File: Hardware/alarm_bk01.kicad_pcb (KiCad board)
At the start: 2 copper layers, 65 x 22 mm, 18 parts, among them Q1 2N3904, SW1 START, SW2 Sensor, SW3 SW_SPDT, U1 ATtiny85V-10P

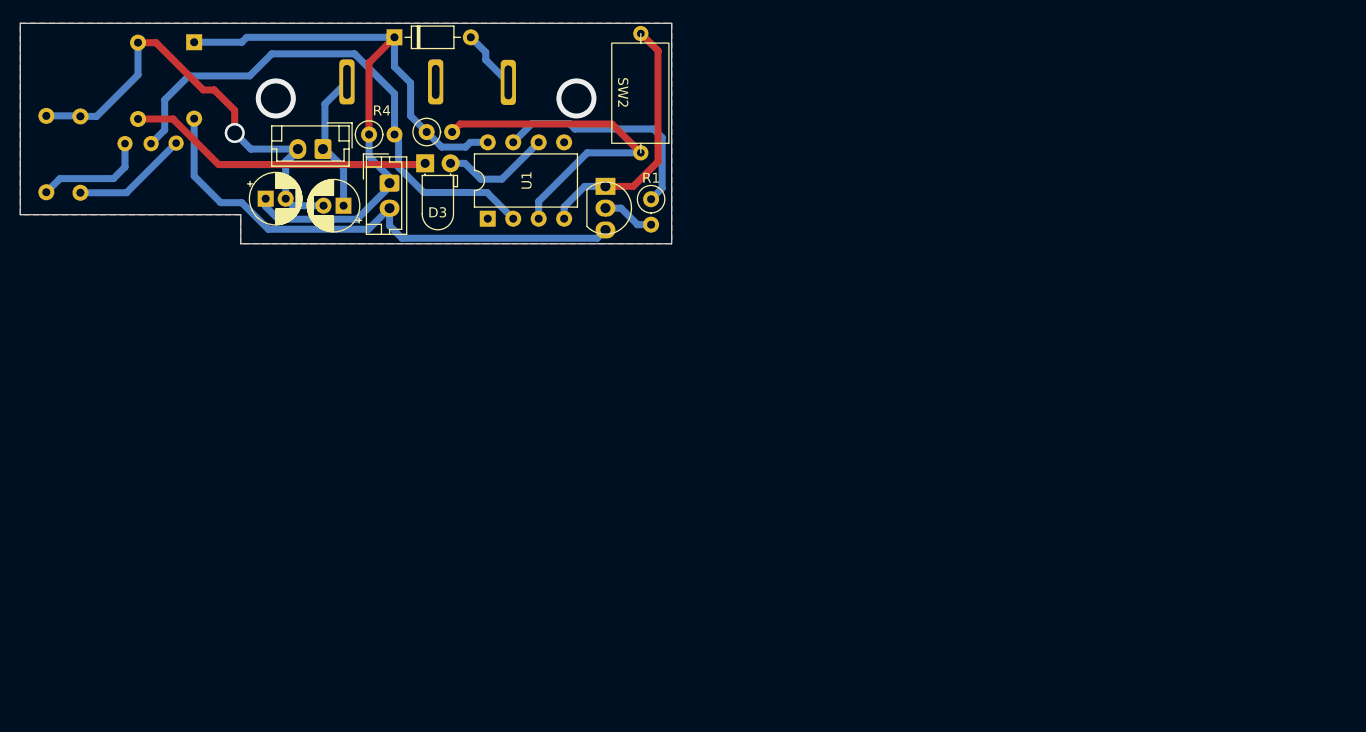
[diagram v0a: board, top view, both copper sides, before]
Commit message: add smd design file
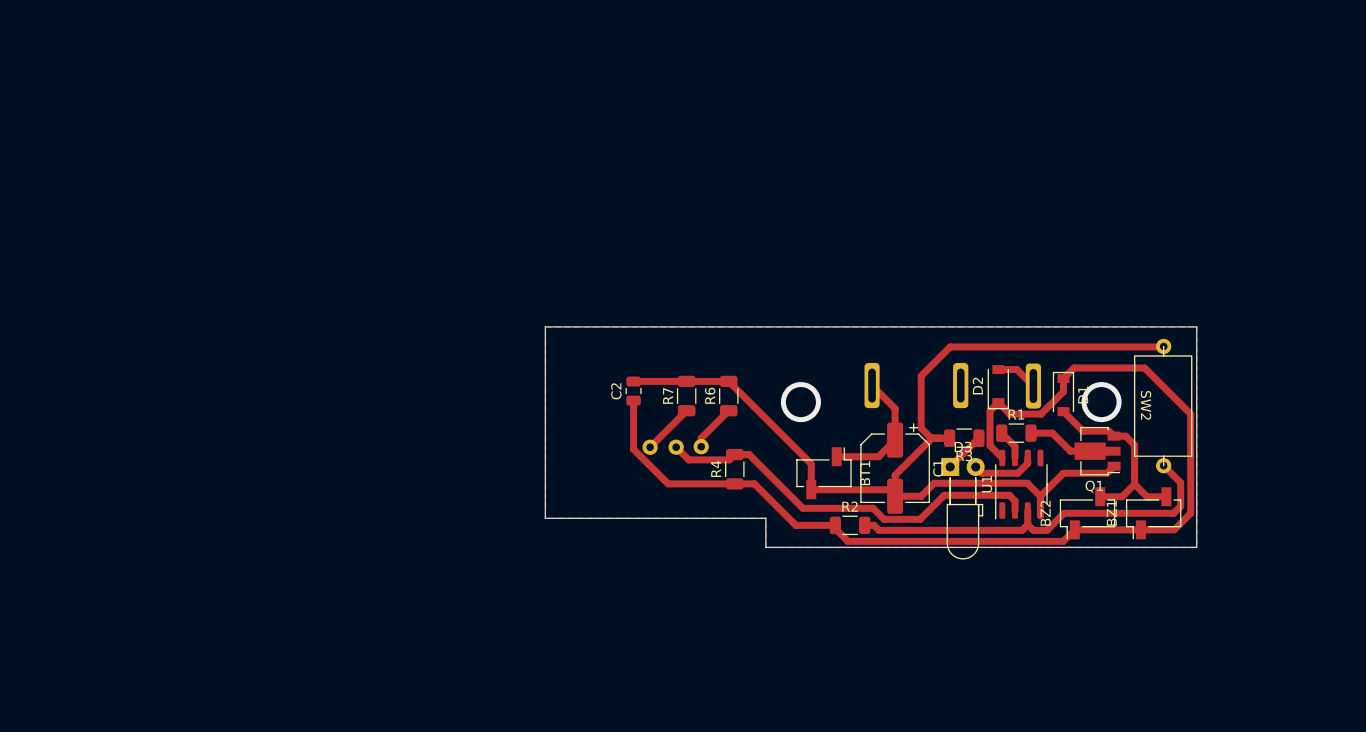
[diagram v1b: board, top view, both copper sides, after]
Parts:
- added BZ2: Buzzer, Connector_PinSocket_2.54mm:PinSocket_1x02_P2.54mm_Vertical_SMD_Pin1Left, F.Cu at (164.3, 80.2)
- BT1, BZ1: footprint Connector_JST:JST_EH_B2B-EH-A_1x02_P2.50mm_Vertical -> Connector_PinSocket_2.54mm:PinSocket_1x02_P2.54mm_Vertical_SMD_Pin1Left
- C1: footprint Capacitor_THT:CP_Radial_D5.0mm_P2.00mm -> Capacitor_SMD:CP_Elec_6.3x5.4
- C2: value 47u -> 47uF; footprint Capacitor_THT:CP_Radial_D5.0mm_P2.00mm -> Capacitor_SMD:C_0805_2012Metric
- D1: footprint Diode_THT:D_DO-35_SOD27_P7.62mm_Horizontal -> Diode_SMD:D_SOD-123; moved to F.Cu
- D2: footprint Diode_THT:D_DO-35_SOD27_P7.62mm_Horizontal -> Diode_SMD:D_SOD-123
- D3: footprint LED_THT:LED_D3.0mm_Horizontal_O1.27mm_Z2.0mm -> LED_THT:LED_D3.0mm_Horizontal_O3.81mm_Z2.0mm
- Q1: footprint custom:TO-92_with_space -> Package_TO_SOT_SMD:SOT-89-3
- R1, R2, R4: footprint Resistor_THT:R_Axial_DIN0207_L6.3mm_D2.5mm_P2.54mm_Vertical -> Resistor_SMD:R_1206_3216Metric
- R3, R6, R7: footprint Resistor_THT:R_Axial_DIN0207_L6.3mm_D2.5mm_P7.62mm_Horizontal -> Resistor_SMD:R_1206_3216Metric; moved to F.Cu
- U1: footprint Package_DIP:DIP-8_W7.62mm -> Package_SO:SOP-8_3.9x4.9mm_P1.27mm
- moved D1 93.6 mm to (161.9, 68.4)
- moved R3 88.4 mm to (152.0, 72.7), turned to 180 degrees
- moved BZ1 83.1 mm to (170.9, 80.2), turned to 90 degrees
- moved D2 69.6 mm to (155.4, 67.5), turned to 90 degrees
- moved R6 67.8 mm to (128.5, 68.5)
- moved R7 67.1 mm to (124.3, 68.5)
- moved C1 61.0 mm to (145.1, 75.7), turned to -90 degrees
- moved SW2 60.8 mm to (171.9, 69.5)
- moved D3 60.5 mm to (150.6, 75.6)
- moved SW3 60.5 mm to (123.2, 76.2)
- moved SW1 60.5 mm to (151.6, 67.5)
- moved BT1 59.6 mm to (138.0, 76.2), turned to -90 degrees
- moved U1 59.5 mm to (157.7, 77.3)
- moved R2 57.7 mm to (140.6, 81.4)
- moved Q1 55.3 mm to (165.3, 74.0), turned to 180 degrees
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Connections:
- SW1 pad COM: /POWER -> (no net)
- SW1 pad NC: /ON_NET -> (no net)
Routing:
- net VCC: track 69.7 -> 106.3 mm
- net Net-(BZ1-Pad2): track 52.5 -> 19.9 mm
- net 0: track 73.6 -> 102.0 mm, vias 1 -> 0
- net Net-(D3-Pad1): track 30.6 -> 4.06 mm
- net alarma: track 22.8 -> 3.02 mm
- net sensibilidad: track 52.8 -> 39.4 mm
- net Net-(R6-Pad1): track 11.6 -> 4.73 mm
- net Net-(R7-Pad1): track 11.2 -> 5.16 mm
- net sensor: track 34.3 -> 39.5 mm
- net Indicator: track 11.0 -> 6.40 mm
- net Net-(Q1-Pad2): track 5.24 -> 8.95 mm
- net /ON_NET: track 6.05 -> 4.18 mm
- net /POWER: track 14.0 -> 12.9 mm
- removed copper zone on B.Cu, net 0

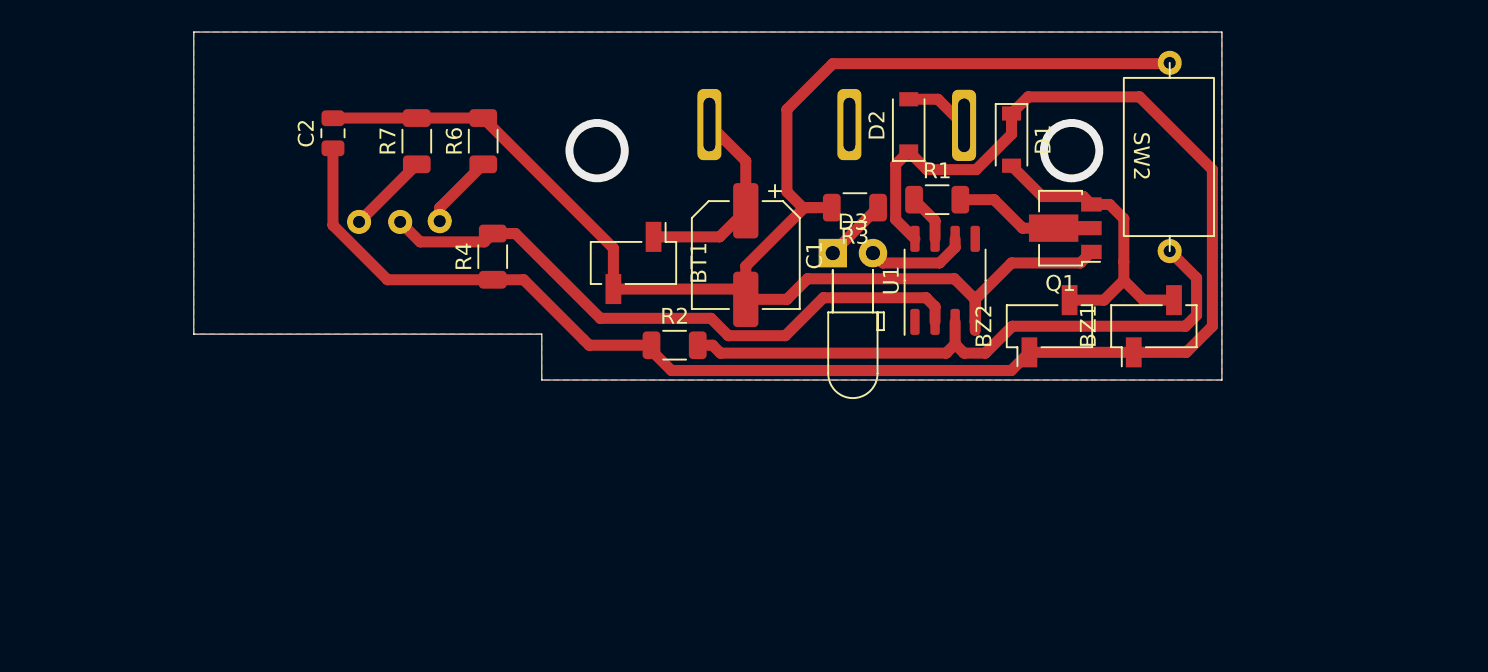
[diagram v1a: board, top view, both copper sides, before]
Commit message: pcb and holes of the new model
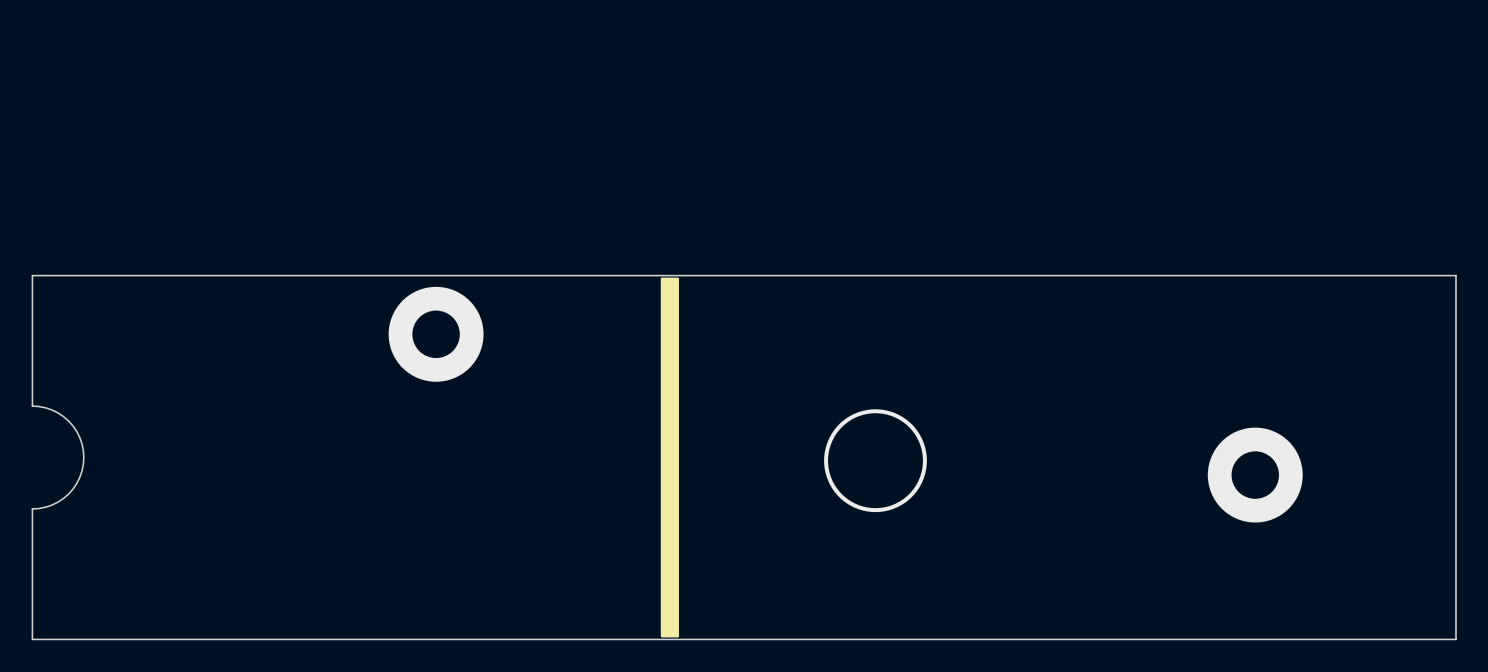
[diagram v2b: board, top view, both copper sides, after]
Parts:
- removed BT1: Battery, Connector_PinSocket_2.54mm:PinSocket_1x02_P2.54mm_Vertical_SMD_Pin1Left
- removed BZ1, BZ2: Buzzer, Connector_PinSocket_2.54mm:PinSocket_1x02_P2.54mm_Vertical_SMD_Pin1Left
- removed C1: 100u, Capacitor_SMD:CP_Elec_6.3x5.4
- removed C2: 47uF, Capacitor_SMD:C_0805_2012Metric
- removed D1, D2: 1N4148, Diode_SMD:D_SOD-123
- removed D3: LED, LED_THT:LED_D3.0mm_Horizontal_O3.81mm_Z2.0mm
- removed Q1: 2N3904, Package_TO_SOT_SMD:SOT-89-3
- removed R1: 180, Resistor_SMD:R_1206_3216Metric
- removed R2: 610k, Resistor_SMD:R_1206_3216Metric
- removed R3: 6.8K, Resistor_SMD:R_1206_3216Metric
- removed R4: 100K, Resistor_SMD:R_1206_3216Metric
- removed R6: LOW, Resistor_SMD:R_1206_3216Metric
- removed R7: HIGH, Resistor_SMD:R_1206_3216Metric
- removed SW1: START, custom:microswitch
- removed SW2: Sensor, custom:WS420
- removed SW3: SW_SPDT, custom:SW-horizontal
- removed U1: ATtiny85V-10P, Package_SO:SOP-8_3.9x4.9mm_P1.27mm
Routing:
- net VCC: track 106.3 -> 0.00 mm
- net 0: track 102.0 -> 0.00 mm
- net sensor: track 39.5 -> 0.00 mm
- net sensibilidad: track 39.4 -> 0.00 mm
- net Net-(BZ1-Pad2): track 19.9 -> 0.00 mm
- net /POWER: track 12.9 -> 0.00 mm
- net Net-(Q1-Pad2): track 8.95 -> 0.00 mm
- net Indicator: track 6.40 -> 0.00 mm
- net Net-(R7-Pad1): track 5.16 -> 0.00 mm
- net Net-(R6-Pad1): track 4.73 -> 0.00 mm
- net /ON_NET: track 4.18 -> 0.00 mm
- net Net-(D3-Pad1): track 4.06 -> 0.00 mm
- net alarma: track 3.02 -> 0.00 mm
- net (no net): vias 2 -> 3
- removed copper zone on F.Cu, net 0
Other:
- board size 65 x 22 mm -> 90 x 23 mm

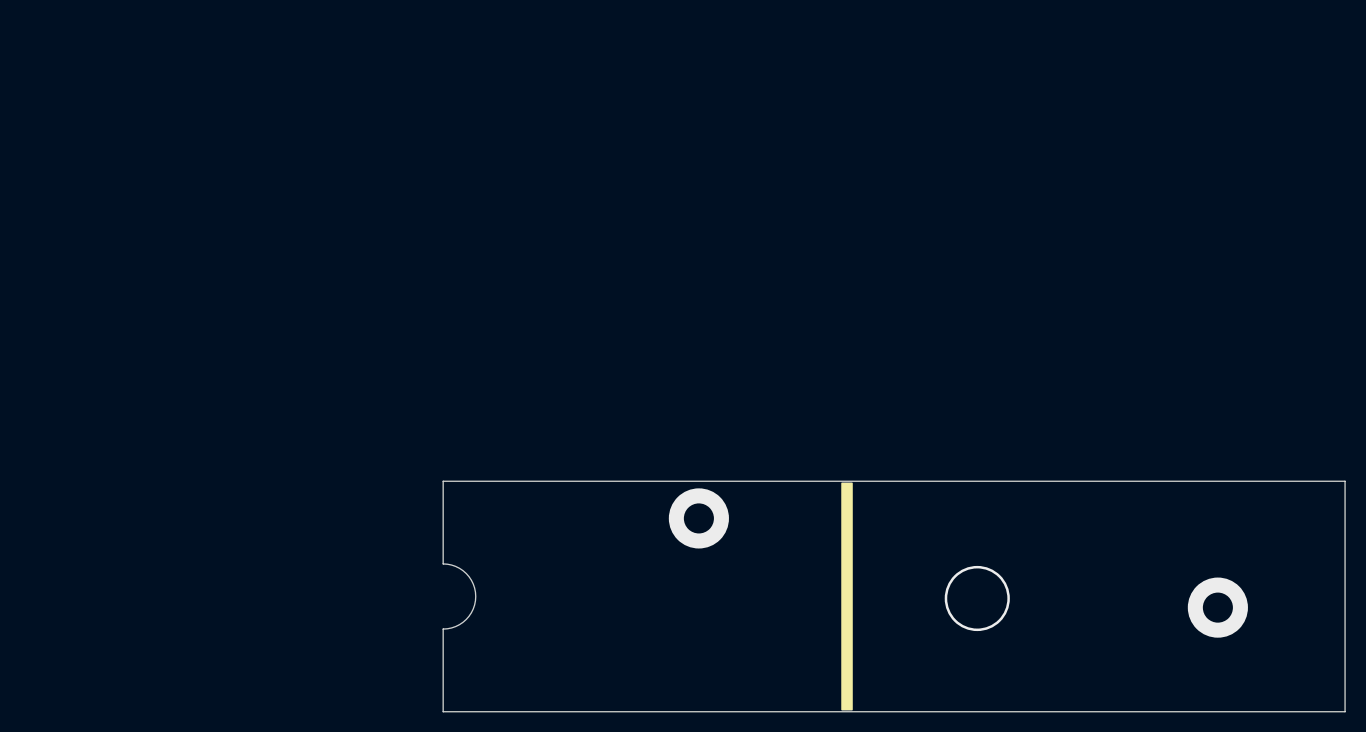
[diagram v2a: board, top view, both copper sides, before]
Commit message: add components locked to pcb
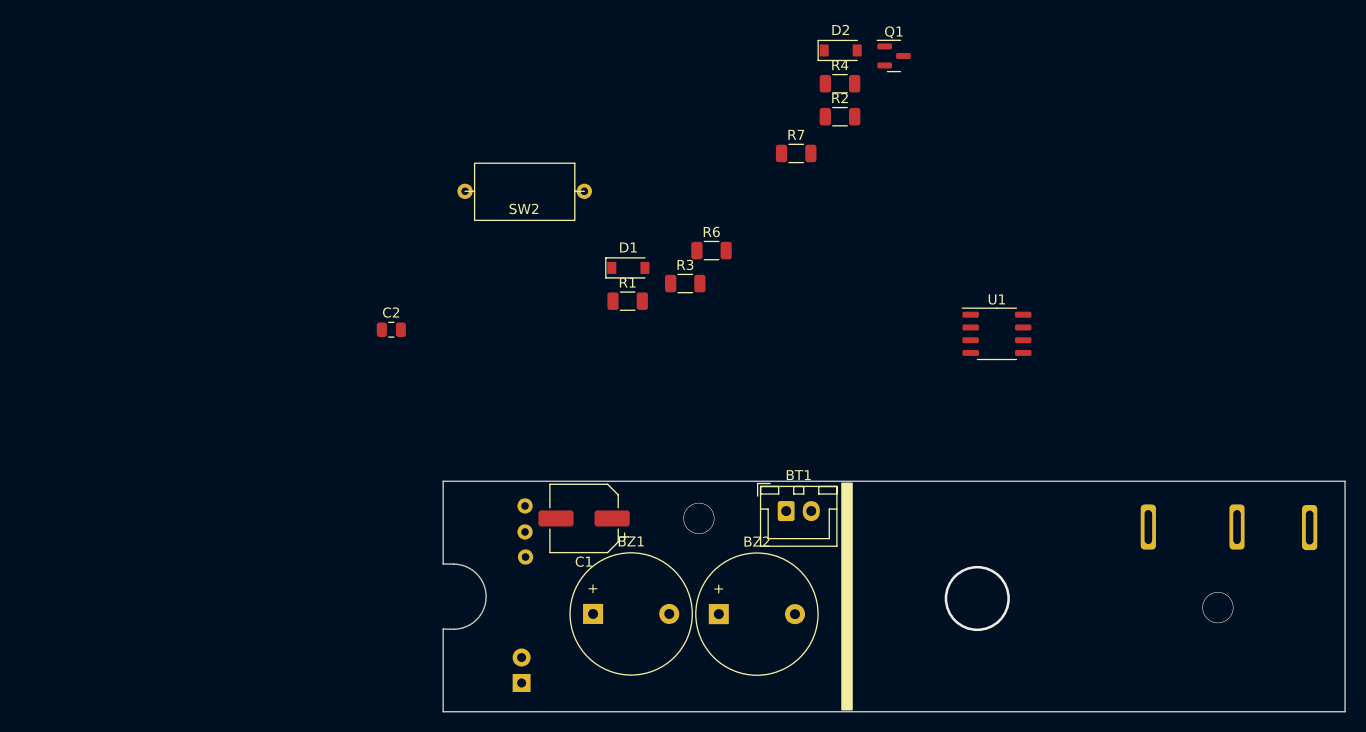
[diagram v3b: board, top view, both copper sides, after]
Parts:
- added BT1: Battery, Connector_JST:JST_XH_B2B-XH-A_1x02_P2.50mm_Vertical, F.Cu at (134.2, 80.0)
- added BZ1: Buzzer, Buzzer_Beeper:Buzzer_12x9.5RM7.6, F.Cu at (115.0, 90.2)
- added BZ2: Buzzer, Buzzer_Beeper:Buzzer_12x9.5RM7.6, F.Cu at (127.5, 90.3)
- added C1: 100u, Capacitor_SMD:CP_Elec_6.3x5.4, F.Cu at (114.1, 80.7)
- added C2: 47uF, Capacitor_SMD:C_0805_2012Metric, F.Cu at (94.8, 61.9)
- added D1: 1N4148, Diode_SMD:D_SOD-123, F.Cu at (118.5, 55.7)
- added D2: 1N4148, Diode_SMD:D_SOD-123, F.Cu at (139.7, 34.0)
- added D3: LED, LED_THT:LED_D3.0mm_Horizontal_O3.81mm_Z2.0mm, B.Cu at (107.8, 97.1)
- added Q1: MMBT3904, Package_TO_SOT_SMD:SOT-23, F.Cu at (145.0, 34.6)
- added R1: 180, Resistor_SMD:R_1206_3216Metric, F.Cu at (118.4, 59.0)
- added R2: 610k, Resistor_SMD:R_1206_3216Metric, F.Cu at (139.6, 40.6)
- added R3: 6.8K, Resistor_SMD:R_1206_3216Metric, F.Cu at (124.2, 57.3)
- added R4: 100K, Resistor_SMD:R_1206_3216Metric, F.Cu at (139.6, 37.3)
- added R6: LOW, Resistor_SMD:R_1206_3216Metric, F.Cu at (126.8, 54.0)
- added R7: HIGH, Resistor_SMD:R_1206_3216Metric, F.Cu at (135.2, 44.3)
- added SW1: START, custom:microswitch, B.Cu at (179.2, 81.6)
- added SW2: Sensor, custom:WS420, F.Cu at (108.1, 48.1)
- added SW3: SW_SPDT, custom:SW-horizontal, B.Cu at (105.6, 82.1)
- added U1: ATtiny85V-10P, Package_SO:SOP-8_3.9x4.9mm_P1.27mm, F.Cu at (155.3, 62.3)
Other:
- outline, holes or cut-outs redrawn

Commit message: Finish smd board
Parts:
- C1: footprint Capacitor_SMD:CP_Elec_6.3x5.4 -> Capacitor_THT:CP_Radial_D5.0mm_P2.50mm
- C2, D1, D2, Q1, R1, R2, R3, R4, R6, R7, U1: moved to B.Cu
- SW2: footprint custom:WS420 -> custom:CX-2548; moved to B.Cu
- moved SW2 91.8 mm to (186.8, 95.4), turned to 90 degrees
- moved C2 83.8 mm to (171.3, 96.2)
- moved R2 67.2 mm to (177.4, 96.1), turned to 90 degrees
- moved Q1 55.7 mm to (145.8, 90.2), turned to 180 degrees
- moved D2 54.3 mm to (164.2, 82.5)
- moved R4 54.2 mm to (162.8, 86.3)
- moved R7 42.5 mm to (113.5, 80.8), turned to -90 degrees
- moved R1 38.7 mm to (148.3, 83.6), turned to 180 degrees
- moved D1 37.4 mm to (143.3, 83.6)
- moved R3 36.2 mm to (110.8, 90.9), turned to 90 degrees
- moved R6 35.9 mm to (110.8, 86.1), turned to -90 degrees
- moved U1 31.7 mm to (165.1, 92.4), turned to 180 degrees
- moved C1 4.72 mm to (118.6, 79.4), turned to -90 degrees
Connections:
- SW1 pad NC: (no net) -> /ON_NET
- SW1 pad NO: (no net) -> /POWER
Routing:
- net 0: track 0.00 -> 192.3 mm
- net VCC: track 0.00 -> 96.7 mm
- net /POWER: track 0.00 -> 76.9 mm, vias 0 -> 1
- net sensibilidad: track 0.00 -> 75.2 mm
- net Indicator: track 0.00 -> 57.7 mm
- net /ON_NET: track 0.00 -> 34.0 mm, vias 0 -> 1
- net Net-(BZ1-Pad2): track 0.00 -> 31.0 mm
- net sensor: track 0.00 -> 20.4 mm
- net alarma: track 0.00 -> 17.5 mm
- net Net-(D3-Pad1): track 0.00 -> 13.2 mm
- net Net-(Q1-Pad1): track 0.00 -> 5.73 mm
- net Net-(R7-Pad1): track 0.00 -> 5.35 mm
- net Net-(R6-Pad1): track 0.00 -> 2.58 mm
- added copper zone on B.Cu, net 0
- added copper zone on F.Cu, net 0

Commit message: last update
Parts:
- C1: footprint Capacitor_THT:CP_Radial_D5.0mm_P2.50mm -> Capacitor_THT:CP_Radial_D6.3mm_P2.50mm
- R2: value 610k -> 10k
- SW1: moved to F.Cu
- U1: value ATtiny85V-10P -> ATtiny85; footprint Package_SO:SOP-8_3.9x4.9mm_P1.27mm -> custom:SOIC127P798X216-8N
- moved R1 1.59 mm to (149.9, 83.6)
- moved D1 1.38 mm to (144.7, 83.6)
- moved BT1 1.10 mm to (133.1, 79.9)
- moved SW2 0.91 mm to (185.8, 95.4)
- moved R7 0.86 mm to (113.4, 80.0), turned to 90 degrees
- moved C2 0.65 mm to (171.8, 96.7), turned to 90 degrees
- moved R6 0.49 mm to (110.8, 86.6)
- moved BZ1 0.46 mm to (114.9, 90.7)
- moved R3 0.37 mm to (110.8, 91.2)
- moved C1 0.20 mm to (118.5, 79.6)
- moved SW1 0.16 mm to (179.1, 81.5)
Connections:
- SW1 pad COM: (no net) -> /POWER
- SW1 pad NO: /POWER -> (no net)
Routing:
- net 0: track 192.3 -> 210.0 mm
- net /POWER: track 76.9 -> 69.5 mm
- net VCC: track 96.7 -> 101.7 mm
- net Net-(BZ1-Pad2): track 31.0 -> 33.0 mm
- net sensor: track 20.4 -> 18.5 mm
- net alarma: track 17.5 -> 15.8 mm
- net Indicator: track 57.7 -> 56.7 mm
- net sensibilidad: track 75.2 -> 74.3 mm
- net Net-(R7-Pad1): track 5.35 -> 6.04 mm
- net Net-(Q1-Pad1): track 5.73 -> 6.42 mm
